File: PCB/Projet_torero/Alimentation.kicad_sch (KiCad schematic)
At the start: 16 parts, among them IC1 MP1475SGJ-P, J2 Conn_01x02, SW3 SW_DPDT_x2, U2 BU33SD5WG-TR

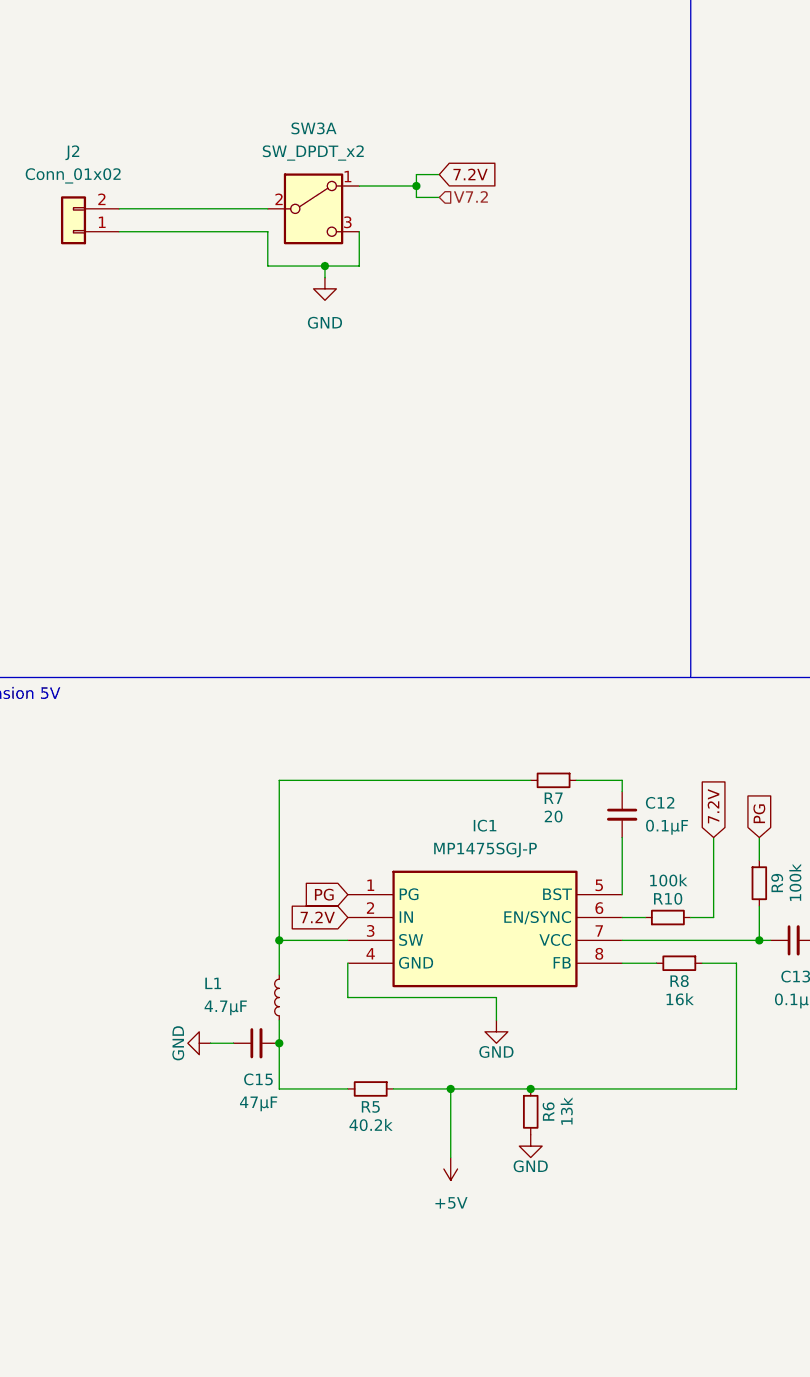
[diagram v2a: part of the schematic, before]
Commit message: modification moteurs et alim
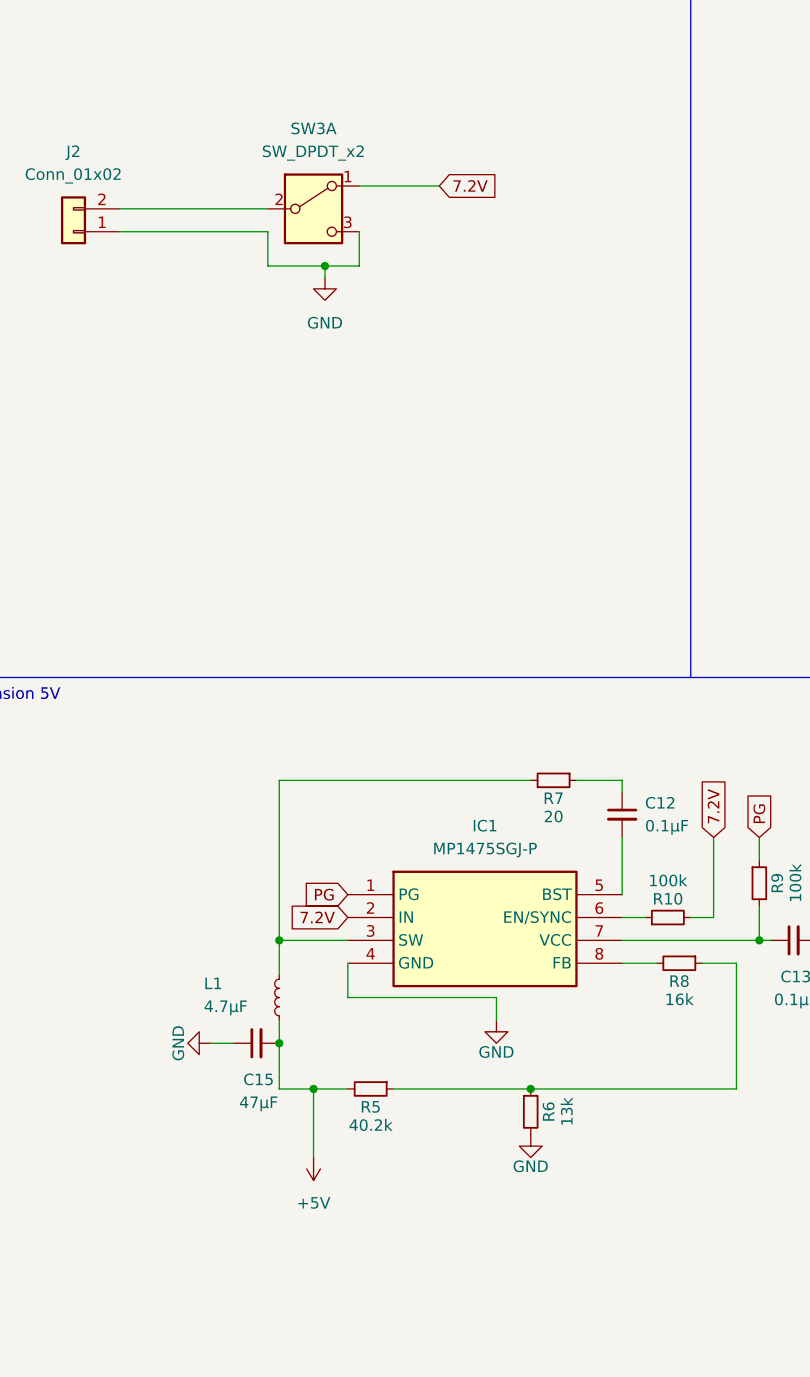
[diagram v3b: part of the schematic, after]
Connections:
- net +5V: now also C15.2, L1.1, R5.2; no longer R5.1, R6.1, R8.1
- new net: R5.1, R6.1, R8.1
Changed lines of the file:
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@@
 	)
 	(junction
-		(at 77.47 135.89)
+		(at 62.23 135.89)
 		(diameter 0)
 		(color 0 0 0 0)
@@
 		(color 0 0 0 0)
 	)
-	(junction
-		(at 73.66 35.56)
-		(diameter 0)
-		(color 0 0 0 0)
-	)
 	(wire
 		(pts
@@
 	(wire
 		(pts
-			(xy 76.2 34.29) (xy 73.66 34.29)
-		)
-		(stroke
-			(width 0)
-			(type default)
-		)
-	)
-	(wire
-		(pts
 			(xy 109.22 121.92) (xy 105.41 121.92)
 		)
@@
 	(wire
 		(pts
-			(xy 77.47 135.89) (xy 77.47 143.51)
-		)
-		(stroke
-			(width 0)
-			(type default)
-		)
-	)
-	(wire
-		(pts
 			(xy 96.52 116.84) (xy 99.06 116.84)
 		)
@@
 	(wire
 		(pts
-			(xy 73.66 34.29) (xy 73.66 35.56)
-		)
-		(stroke
-			(width 0)
-			(type default)
-		)
-	)
-	(wire
-		(pts
 			(xy 63.5 44.45) (xy 63.5 45.72)
 		)
@@
 	(wire
 		(pts
-			(xy 73.66 35.56) (xy 73.66 36.83)
+			(xy 62.23 135.89) (xy 62.23 143.51)
 		)
 		(stroke
@@
 	(wire
 		(pts
-			(xy 58.42 135.89) (xy 66.04 135.89)
-		)
-		(stroke
-			(width 0)
-			(type default)
-		)
-	)
-	(wire
-		(pts
-			(xy 67.31 35.56) (xy 73.66 35.56)
-		)
-		(stroke
-			(width 0)
-			(type default)
-		)
-	)
-	(wire
-		(pts
-			(xy 71.12 135.89) (xy 77.47 135.89)
+			(xy 58.42 135.89) (xy 62.23 135.89)
+		)
+		(stroke
+			(width 0)
+			(type default)
+		)
+	)
+	(wire
+		(pts
+			(xy 67.31 35.56) (xy 76.2 35.56)
+		)
+		(stroke
+			(width 0)
+			(type default)
+		)
+	)
+	(wire
+		(pts
+			(xy 71.12 135.89) (xy 86.36 135.89)
 		)
 		(stroke
@@
 	(wire
 		(pts
-			(xy 73.66 36.83) (xy 76.2 36.83)
-		)
-		(stroke
-			(width 0)
-			(type default)
-		)
-	)
-	(wire
-		(pts
-			(xy 77.47 135.89) (xy 86.36 135.89)
+			(xy 62.23 135.89) (xy 66.04 135.89)
 		)
 		(stroke
@@
 	(global_label "7.2V"
 		(shape input)
-		(at 76.2 34.29 0)
+		(at 76.2 35.56 0)
 		(fields_autoplaced yes)
 		(effects
@@
 		)
 		(property "Intersheetrefs" "${INTERSHEET_REFS}"
-			(at 83.2976 34.29 0)
+			(at 83.2976 35.56 0)
 			(effects
 				(font
@@
 		)
 	)
-	(hierarchical_label "V7.2"
-		(shape input)
-		(at 76.2 36.83 0)
-		(fields_autoplaced yes)
-		(effects
-			(font
-				(size 1.27 1.27)
-			)
-			(justify left)
-		)
-	)
 	(symbol
 		(lib_id "power:+3.3V")
@@
 	)
 	(symbol
+		(lib_id "power:+5V")
+		(at 62.23 143.51 180)
+		(unit 1)
+		(exclude_from_sim no)
+		(in_bom yes)
+		(on_board yes)
+		(dnp no)
+		(fields_autoplaced yes)
+		(property "Reference" "#PWR0501"
+			(at 62.23 139.7 0)
+			(effects
+				(font
+					(size 1.27 1.27)
+				)
+				(hide yes)
+			)
+		)
+		(property "Value" "+5V"
+			(at 62.23 148.59 0)
+			(effects
+				(font
+					(size 1.27 1.27)
+				)
+			)
+		)
+		(property "Footprint" ""
+			(at 62.23 143.51 0)
+			(effects
+				(font
+					(size 1.27 1.27)
+				)
+				(hide yes)
+			)
+		)
+		(property "Datasheet" ""
+			(at 62.23 143.51 0)
+			(effects
+				(font
+					(size 1.27 1.27)
+				)
+				(hide yes)
+			)
+		)
+		(property "Description" "Power symbol creates a global label with name \"+5V\""
+			(at 62.23 143.51 0)
+			(effects
+				(font
+					(size 1.27 1.27)
+				)
+				(hide yes)
+			)
+		)
+		(pin "1"
+		)
+		(instances
+			(project "Projet_torero"
+				(path "/04e1eb47-a2c4-462b-bef7-377d9515a2c0/b3b2826c-2e3c-42fe-bcd6-22fcd6249c25"
+					(reference "#PWR0501")
+					(unit 1)
+				)
+			)
+		)
+	)
+	(symbol
 		(lib_id "Device:R_Small")
 		(at 111.76 113.03 0)
@@
 					(unit 1)
 				)
-			)
-		)
-	)
-	(symbol
-		(lib_id "power:+5V")
-		(at 77.47 143.51 180)
-		(unit 1)
-		(exclude_from_sim no)
-		(in_bom yes)
-		(on_board yes)
-		(dnp no)
-		(fields_autoplaced yes)
-		(property "Reference" "#PWR024"
-			(at 77.47 139.7 0)
-			(effects
-				(font
-					(size 1.27 1.27)
-				)
-				(hide yes)
-			)
-		)
-		(property "Value" "+5V"
-			(at 77.47 148.59 0)
-			(effects
-				(font
-					(size 1.27 1.27)
-				)
-			)
-		)
-		(property "Footprint" ""
-			(at 77.47 143.51 0)
-			(effects
-				(font
-					(size 1.27 1.27)
-				)
-				(hide yes)
-			)
-		)
-		(property "Datasheet" ""
-			(at 77.47 143.51 0)
-			(effects
-				(font
-					(size 1.27 1.27)
-				)
-				(hide yes)
-			)
-		)
-		(property "Description" "Power symbol creates a global label with name \"+5V\""
-			(at 77.47 143.51 0)
-			(effects
-				(font
-					(size 1.27 1.27)
-				)
-				(hide yes)
-			)
-		)
-		(pin "1"
-		)
-		(instances
-			(project "Projet_torero"
-				(path "/04e1eb47-a2c4-462b-bef7-377d9515a2c0/b3b2826c-2e3c-42fe-bcd6-22fcd6249c25"
-					(reference "#PWR024")
-					(unit 1)
-				)
